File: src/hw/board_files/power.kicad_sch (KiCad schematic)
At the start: 38 parts, among them J1 Conn_01x03_Pin, P1 USB_C_Plug_USB2.0, SW1 SW_PWR, U1 FT234XD-R, U2 MCP73871, U3 TPS63031DSKR

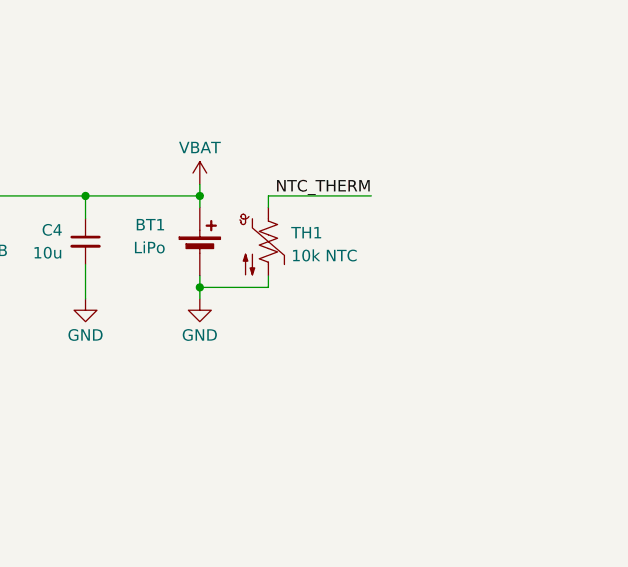
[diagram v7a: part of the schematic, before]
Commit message: Moved some things around, revised regulator layout
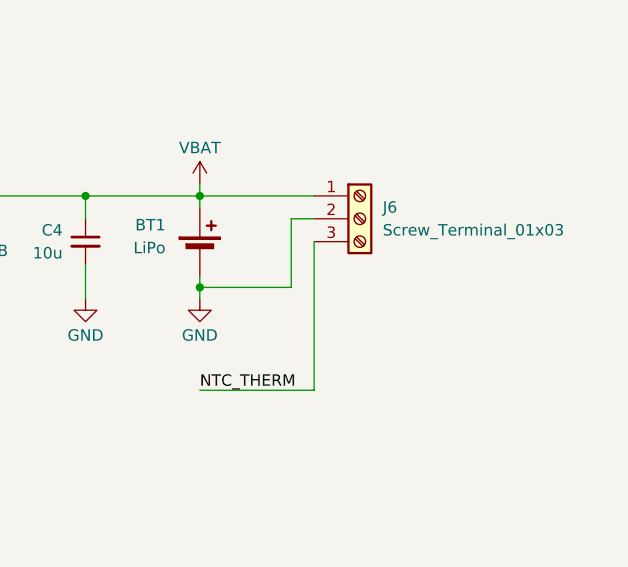
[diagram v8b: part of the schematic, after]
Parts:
- removed TH1: 10k NTC, symbol Device:Thermistor_NTC_US
- added J6: Screw_Terminal_01x03, TerminalBlock_Phoenix:TerminalBlock_Phoenix_MPT-0,5-3-2.54_1x03_P2.54mm_Horizontal, symbol Connector:Screw_Terminal_01x03
- NT1: footprint (none) -> NetTie:NetTie-2_SMD_Pad0.5mm
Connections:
- net GND: now also J6.2 (Pin_2)
- net NTC_THERM: now also J6.3 (Pin_3)
- net VBAT: now also J6.1 (Pin_1)
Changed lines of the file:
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@@
 	)
 	(junction
+		(at 250.19 135.89)
+		(diameter 0)
+		(color 0 0 0 0)
+	)
+	(junction
 		(at 148.59 80.01)
 		(diameter 0)
@@
 	)
 	(junction
-		(at 250.19 135.89)
-		(diameter 0)
-		(color 0 0 0 0)
-	)
-	(junction
 		(at 132.08 48.26)
 		(diameter 0)
@@
 	(wire
 		(pts
-			(xy 257.81 134.62) (xy 257.81 135.89)
-		)
-		(stroke
-			(width 0)
-			(type default)
-		)
-	)
-	(wire
-		(pts
 			(xy 55.88 82.55) (xy 55.88 90.17)
 		)
@@
 	(wire
 		(pts
-			(xy 250.19 135.89) (xy 250.19 137.16)
-		)
-		(stroke
-			(width 0)
-			(type default)
-		)
-	)
-	(wire
-		(pts
 			(xy 105.41 153.67) (xy 111.76 153.67)
 		)
@@
 	(wire
 		(pts
+			(xy 262.89 130.81) (xy 262.89 147.32)
+		)
+		(stroke
+			(width 0)
+			(type default)
+		)
+	)
+	(wire
+		(pts
+			(xy 262.89 128.27) (xy 260.35 128.27)
+		)
+		(stroke
+			(width 0)
+			(type default)
+		)
+	)
+	(wire
+		(pts
 			(xy 35.56 152.4) (xy 29.21 152.4)
 		)
@@
 	(wire
 		(pts
-			(xy 67.31 67.31) (xy 97.79 67.31)
+			(xy 250.19 147.32) (xy 262.89 147.32)
 		)
 		(stroke
@@
 	(wire
 		(pts
-			(xy 80.01 49.53) (xy 67.31 49.53)
+			(xy 67.31 67.31) (xy 97.79 67.31)
 		)
 		(stroke
@@
 	(wire
 		(pts
-			(xy 224.79 148.59) (xy 226.06 148.59)
+			(xy 80.01 49.53) (xy 67.31 49.53)
 		)
 		(stroke
@@
 	(wire
 		(pts
-			(xy 218.44 118.11) (xy 218.44 119.38)
+			(xy 224.79 148.59) (xy 226.06 148.59)
 		)
 		(stroke
@@
 	(wire
 		(pts
-			(xy 110.49 55.88) (xy 106.68 55.88)
+			(xy 218.44 118.11) (xy 218.44 119.38)
 		)
 		(stroke
@@
 	(wire
 		(pts
-			(xy 257.81 135.89) (xy 250.19 135.89)
+			(xy 110.49 55.88) (xy 106.68 55.88)
 		)
 		(stroke
@@
 	(wire
 		(pts
+			(xy 250.19 135.89) (xy 250.19 137.16)
+		)
+		(stroke
+			(width 0)
+			(type default)
+		)
+	)
+	(wire
+		(pts
 			(xy 204.47 158.75) (xy 208.28 158.75)
 		)
@@
 	(wire
 		(pts
+			(xy 260.35 128.27) (xy 260.35 135.89)
+		)
+		(stroke
+			(width 0)
+			(type default)
+		)
+	)
+	(wire
+		(pts
 			(xy 204.47 125.73) (xy 237.49 125.73)
 		)
@@
 	(wire
 		(pts
-			(xy 257.81 127) (xy 257.81 125.73)
-		)
-		(stroke
-			(width 0)
-			(type default)
-		)
-	)
-	(wire
-		(pts
 			(xy 16.51 151.13) (xy 16.51 152.4)
 		)
@@
 	(wire
 		(pts
+			(xy 260.35 135.89) (xy 250.19 135.89)
+		)
+		(stroke
+			(width 0)
+			(type default)
+		)
+	)
+	(wire
+		(pts
 			(xy 132.08 74.93) (xy 133.35 74.93)
 		)
@@
 	(wire
 		(pts
-			(xy 257.81 125.73) (xy 269.24 125.73)
+			(xy 250.19 125.73) (xy 262.89 125.73)
 		)
 		(stroke
@@
 	)
 	(label "NTC_THERM"
-		(at 269.24 125.73 180)
+		(at 250.19 147.32 0)
 		(effects
 			(font
 				(size 1.27 1.27)
 			)
-			(justify right bottom)
+			(justify left bottom)
 		)
 	)
@@
 	)
 	(symbol
-		(lib_id "Device:Thermistor_NTC_US")
-		(at 257.81 130.81 0)
-		(unit 1)
-		(exclude_from_sim no)
-		(in_bom no)
-		(on_board no)
-		(dnp no)
-		(fields_autoplaced yes)
-		(property "Reference" "TH1"
-			(at 260.35 129.8574 0)
-			(effects
-				(font
-					(size 1.27 1.27)
-				)
-				(justify left)
-			)
-		)
-		(property "Value" "10k NTC"
-			(at 260.35 132.3974 0)
-			(effects
-				(font
-					(size 1.27 1.27)
-				)
-				(justify left)
-			)
-		)
-		(property "Footprint" ""
-			(at 257.81 129.54 0)
-			(effects
-				(font
-					(size 1.27 1.27)
-				)
-				(hide yes)
-			)
-		)
-		(property "Datasheet" "~"
-			(at 257.81 129.54 0)
-			(effects
-				(font
-					(size 1.27 1.27)
-				)
-				(hide yes)
-			)
-		)
-		(property "Description" "Temperature dependent resistor, negative temperature coefficient, US symbol"
-			(at 257.81 130.81 0)
-			(effects
-				(font
-					(size 1.27 1.27)
-				)
-				(hide yes)
-			)
-		)
-		(pin "1"
-		)
-		(pin "2"
-		)
-		(instances
-			(project ""
-				(path "/2c77a8ba-b277-4959-adec-d3fc778c7960/7763c5b3-a08f-479a-9f6f-ea394e6f7159"
-					(reference "TH1")
-					(unit 1)
-				)
-			)
-		)
-	)
-	(symbol
 		(lib_id "power:GND")
 		(at 81.28 96.52 0)
@@
 			)
 		)
-		(property "Footprint" ""
+		(property "Footprint" "NetTie:NetTie-2_SMD_Pad0.5mm"
 			(at 92.71 195.58 0)
 			(effects
@@
 	)
 	(symbol
+		(lib_id "Connector:Screw_Terminal_01x03")
+		(at 267.97 128.27 0)
+		(unit 1)
+		(exclude_from_sim no)
+		(in_bom yes)
+		(on_board yes)
+		(dnp no)
+		(fields_autoplaced yes)
+		(property "Reference" "J6"
+			(at 270.51 126.9999 0)
+			(effects
+				(font
+					(size 1.27 1.27)
+				)
+				(justify left)
+			)
+		)
+		(property "Value" "Screw_Terminal_01x03"
+			(at 270.51 129.5399 0)
+			(effects
+				(font
+					(size 1.27 1.27)
+				)
+				(justify left)
+			)
+		)
+		(property "Footprint" "TerminalBlock_Phoenix:TerminalBlock_Phoenix_MPT-0,5-3-2.54_1x03_P2.54mm_Horizontal"
+			(at 267.97 128.27 0)
+			(effects
+				(font
+					(size 1.27 1.27)
+				)
+				(hide yes)
+			)
+		)
+		(property "Datasheet" "~"
+			(at 267.97 128.27 0)
+			(effects
+				(font
+					(size 1.27 1.27)
+				)
+				(hide yes)
+			)
+		)
+		(property "Description" "Generic screw terminal, single row, 01x03, script generated (kicad-library-utils/schlib/autogen/connector/)"
+			(at 267.97 128.27 0)
+			(effects
+				(font
+					(size 1.27 1.27)
+				)
+				(hide yes)
+			)
+		)
+		(pin "1"
+		)
+		(pin "2"
+		)
+		(pin "3"
+		)
+		(instances
+			(project ""
+				(path "/2c77a8ba-b277-4959-adec-d3fc778c7960/7763c5b3-a08f-479a-9f6f-ea394e6f7159"
+					(reference "J6")
+					(unit 1)
+				)
+			)
+		)
+	)
+	(symbol
 		(lib_id "power:+3V3")
 		(at 16.51 151.13 0)
@@
 		(exclude_from_sim no)
 		(in_bom yes)
-		(on_board yes)
+		(on_board no)
 		(dnp no)
 		(fields_autoplaced yes)
